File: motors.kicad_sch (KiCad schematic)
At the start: 28 parts, among them Q1 NMOS, Q2 NMOS, Q3 NMOS, Q4 NMOS

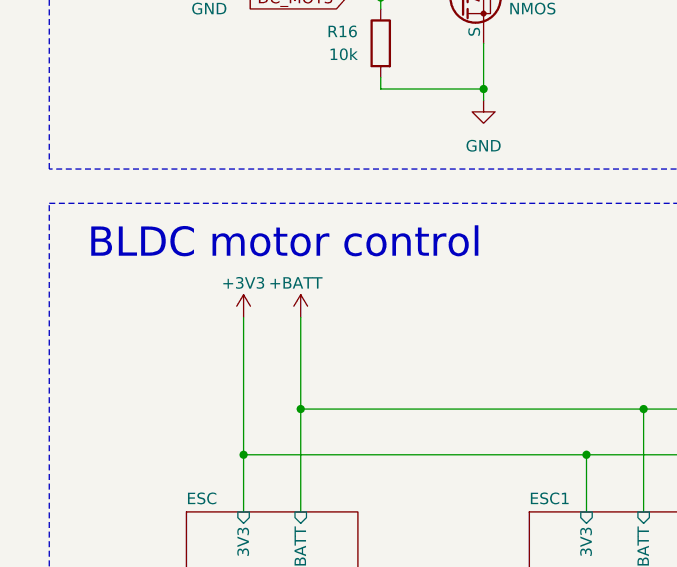
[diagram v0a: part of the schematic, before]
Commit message: Merge peripherals and sensors sheets
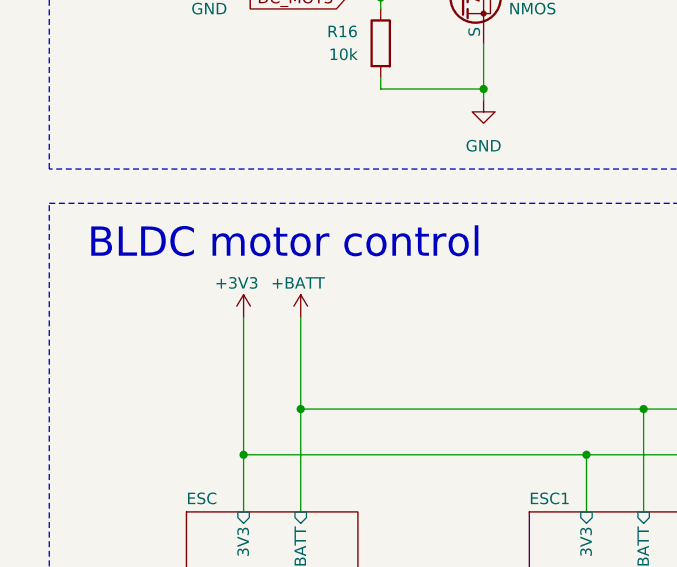
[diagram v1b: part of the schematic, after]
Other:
- company: (none) -> All-in-one drone flight controller, camera and ESC
- title: (none) -> Anticopter Duo
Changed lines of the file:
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@@
 	(generator_version "10.0")
 	(paper "A4")
+	(title_block
+		(title "Anticopter Duo")
+		(date "2026-08-28")
+		(rev "1.0")
+		(company "All-in-one drone flight controller, camera and ESC")
+		(comment 1 "ESP32 P4 + ESP32 C5, 4xAM32 ESCs")
+		(comment 2 "1S DC motors, 2S-3S BLDC motors")
+	)
 	(rectangle
 		(start 17.78 115.57)
@@
 	)
 	(junction
-		(at 39.37 143.51)
+		(at 45.72 138.43)
 		(diameter 0)
 		(color 0 0 0 0)
@@
 	)
 	(junction
-		(at 45.72 138.43)
-		(diameter 0)
-		(color 0 0 0 0)
-	)
-	(junction
 		(at 60.96 33.02)
 		(diameter 0)
@@
 	)
 	(junction
+		(at 39.37 143.51)
+		(diameter 0)
+		(color 0 0 0 0)
+	)
+	(junction
 		(at 90.17 76.2)
 		(diameter 0)
@@
 		)
 		(property "Value" "+3V3"
-			(at 39.37 124.46 0)
+			(at 38.608 124.46 0)
 			(show_name no)
 			(do_not_autoplace no)
@@
 		)
 		(property "Value" "+BATT"
-			(at 42.164 124.46 0)
+			(at 42.418 124.46 0)
 			(show_name no)
 			(do_not_autoplace no)

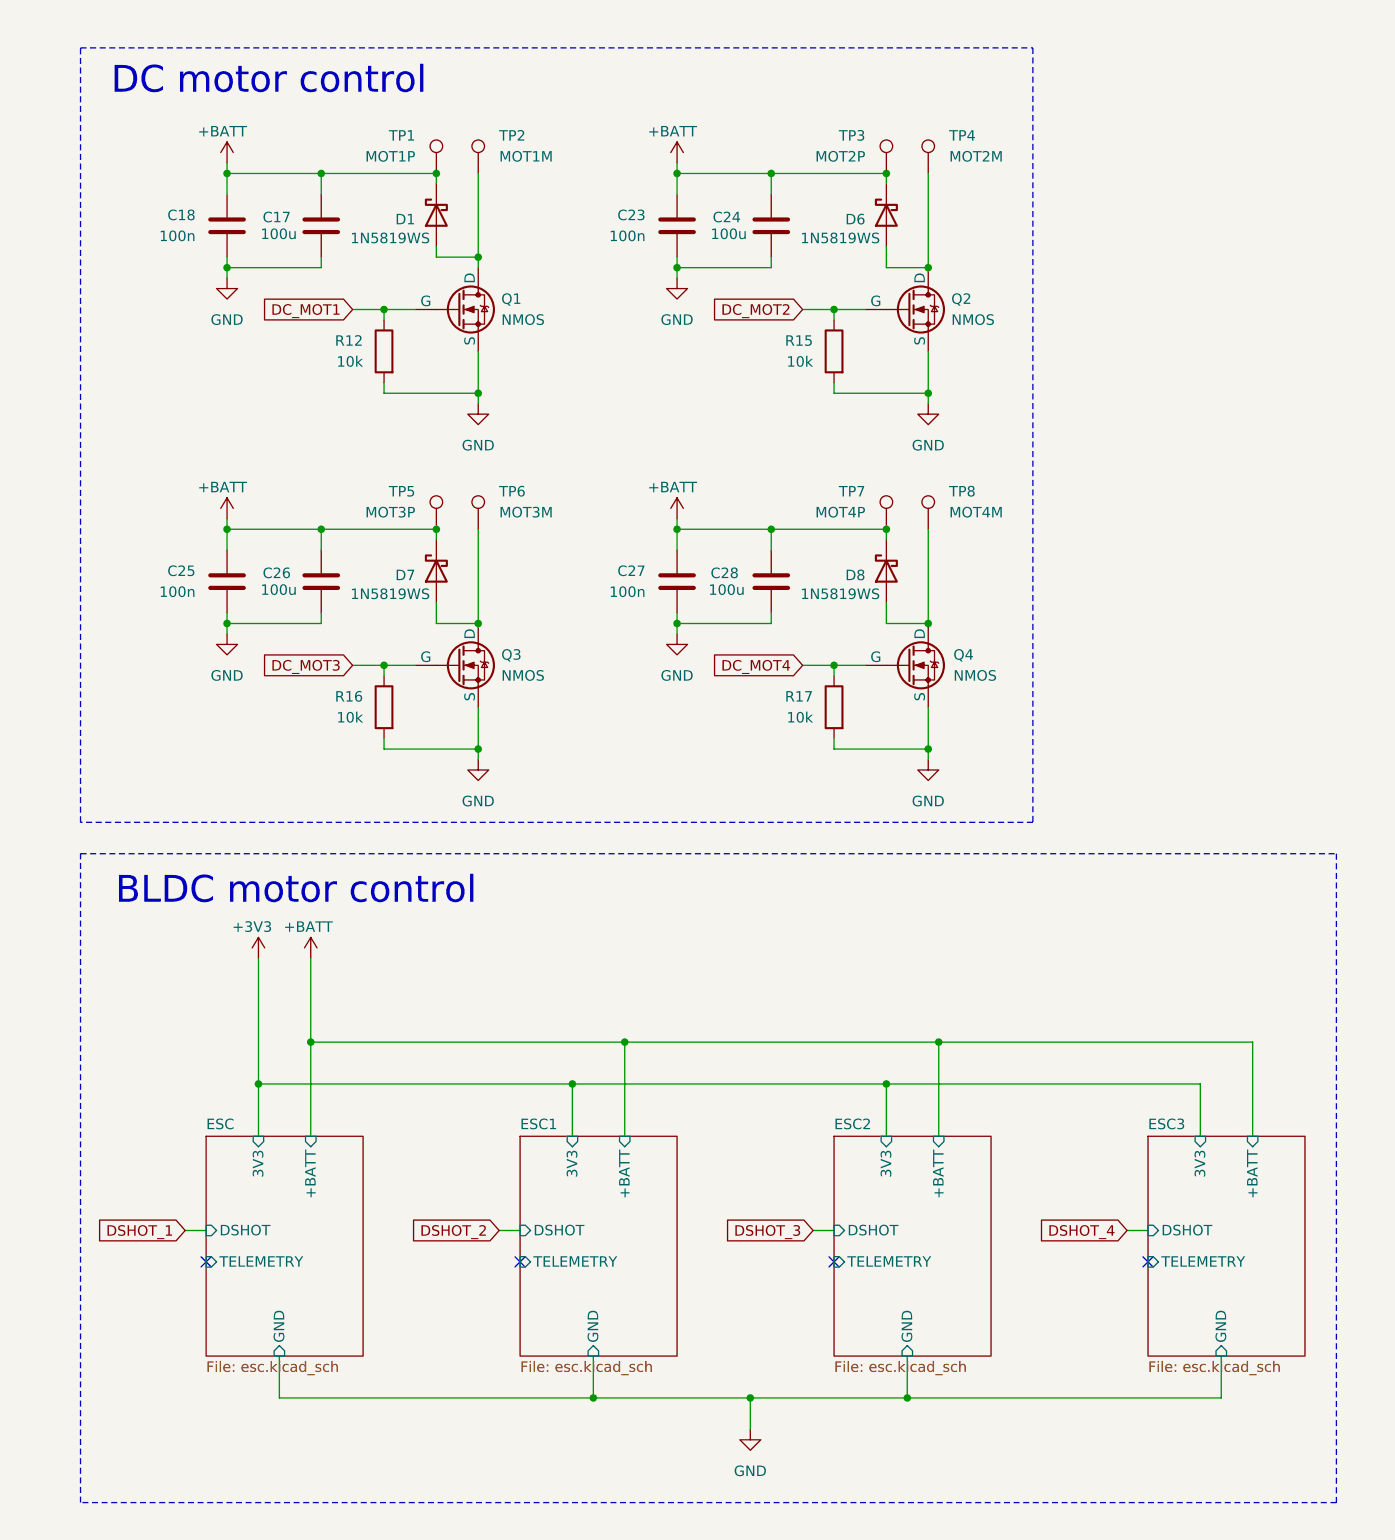
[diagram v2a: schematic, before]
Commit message: Prettify most of the schematics
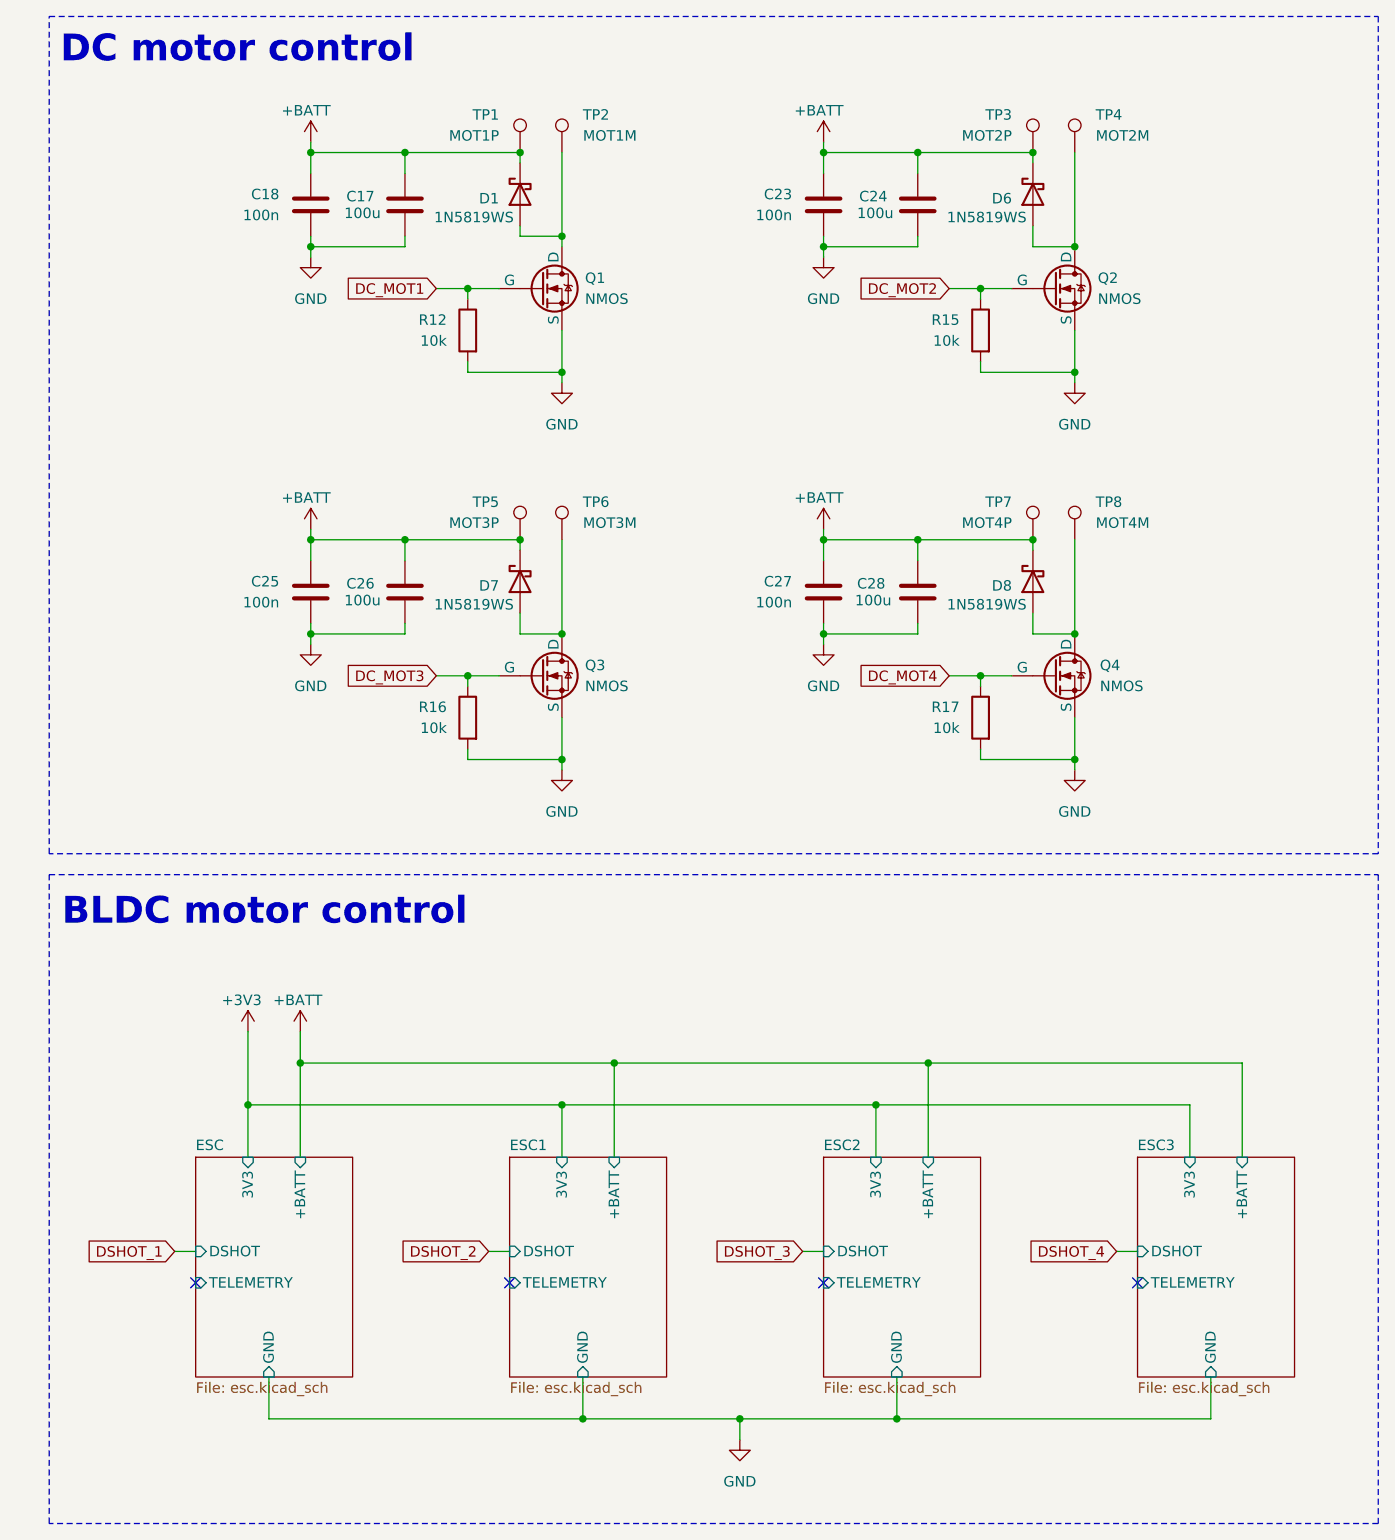
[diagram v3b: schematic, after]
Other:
- moved on the sheet: C17, C18, C23, C24, C25, C26, C27, C28, D1, D6, D7, D8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

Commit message: Various schematic improvements
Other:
- note added: "BLDC Motor Control"
- note added: "DC Motor Control"
- note removed: "BLDC motor control"
- note removed: "DC motor control"
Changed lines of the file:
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@@
 		)
 	)
-	(text "DC motor control"
+	(text "DC Motor Control"
 		(exclude_from_sim no)
 		(at 36.83 18.034 0)
@@
 		)
 	)
-	(text "BLDC motor control"
+	(text "BLDC Motor Control"
 		(exclude_from_sim no)
 		(at 40.132 122.682 0)

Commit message: Fix USB 5v -> VBUS error and some other small things
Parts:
- added R186: 10, Resistor_SMD:R_0603_1608Metric, symbol Device:R
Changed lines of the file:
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@@
 	(wire
 		(pts
-			(xy 60.96 46.99) (xy 64.77 46.99)
+			(xy 62.23 46.99) (xy 64.77 46.99)
 		)
 		(stroke
@@
 	(global_label "DC_MOT1"
 		(shape input)
-		(at 60.96 46.99 180)
+		(at 62.23 46.99 180)
 		(fields_autoplaced yes)
 		(effects
@@
 		)
 		(property "Intersheetrefs" "${INTERSHEET_REFS}"
-			(at 49.5082 46.99 0)
+			(at 50.7782 46.99 0)
 			(hide yes)
 			(show_name no)
@@
 					(unit 1)
 				)
+			)
+		)
+	)
+	(symbol
+		(lib_id "Device:R")
+		(at 55.88 64.77 270)
+		(mirror x)
+		(unit 1)
+		(body_style 1)
+		(exclude_from_sim no)
+		(in_bom yes)
+		(on_board yes)
+		(in_pos_files yes)
+		(dnp no)
+		(property "Reference" "R186"
+			(at 55.88 69.85 90)
+			(show_name no)
+			(do_not_autoplace no)
+			(effects
+				(font
+					(size 1.27 1.27)
+				)
+			)
+		)
+		(property "Value" "10"
+			(at 55.88 67.31 90)
+			(show_name no)
+			(do_not_autoplace no)
+			(effects
+				(font
+					(size 1.27 1.27)
+				)
+			)
+		)
+		(property "Footprint" "Resistor_SMD:R_0603_1608Metric"
+			(at 55.88 66.548 90)
+			(hide yes)
+			(show_name no)
+			(do_not_autoplace no)
+			(effects
+				(font
+					(size 1.27 1.27)
+				)
+			)
+		)
+		(property "Datasheet" ""
+			(at 55.88 64.77 0)
+			(hide yes)
+			(show_name no)
+			(do_not_autoplace no)
+			(effects
+				(font
+					(size 1.27 1.27)
+				)
+			)
+		)
+		(property "Description" "Resistor"
+			(at 55.88 64.77 0)
+			(hide yes)
+			(show_name no)
+			(do_not_autoplace no)
+			(effects
+				(font
+					(size 1.27 1.27)
+				)
+			)
+		)
+		(pin "2"
+		)
+		(pin "1"
+		)
+		(instances
+			(project "espdrone"
+				(path "/d7b09c1f-60ff-44c2-9b85-8e9b4c9b8de4"
+					(reference "R186")
+					(unit 1)
+				)

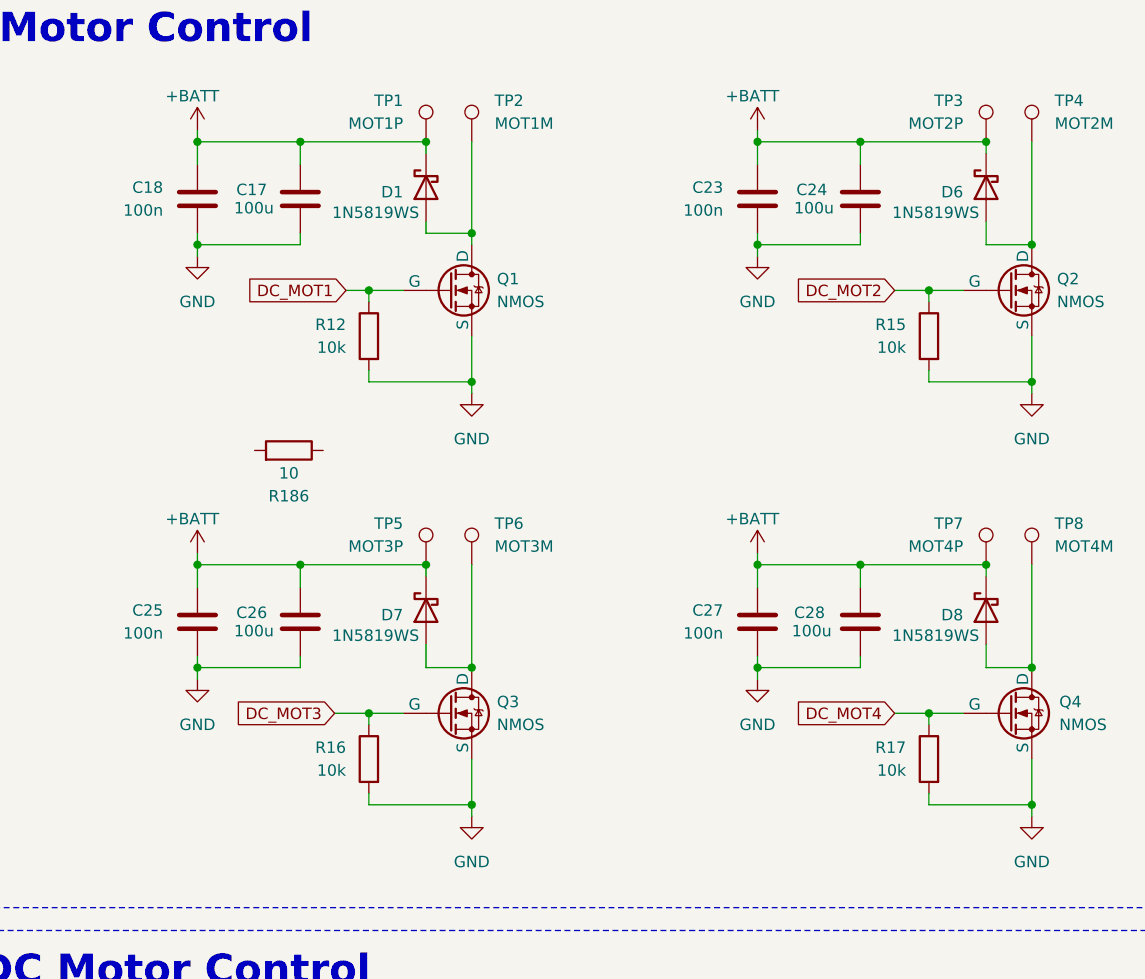
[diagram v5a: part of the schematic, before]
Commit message: Improve connectors and DC flyback diode
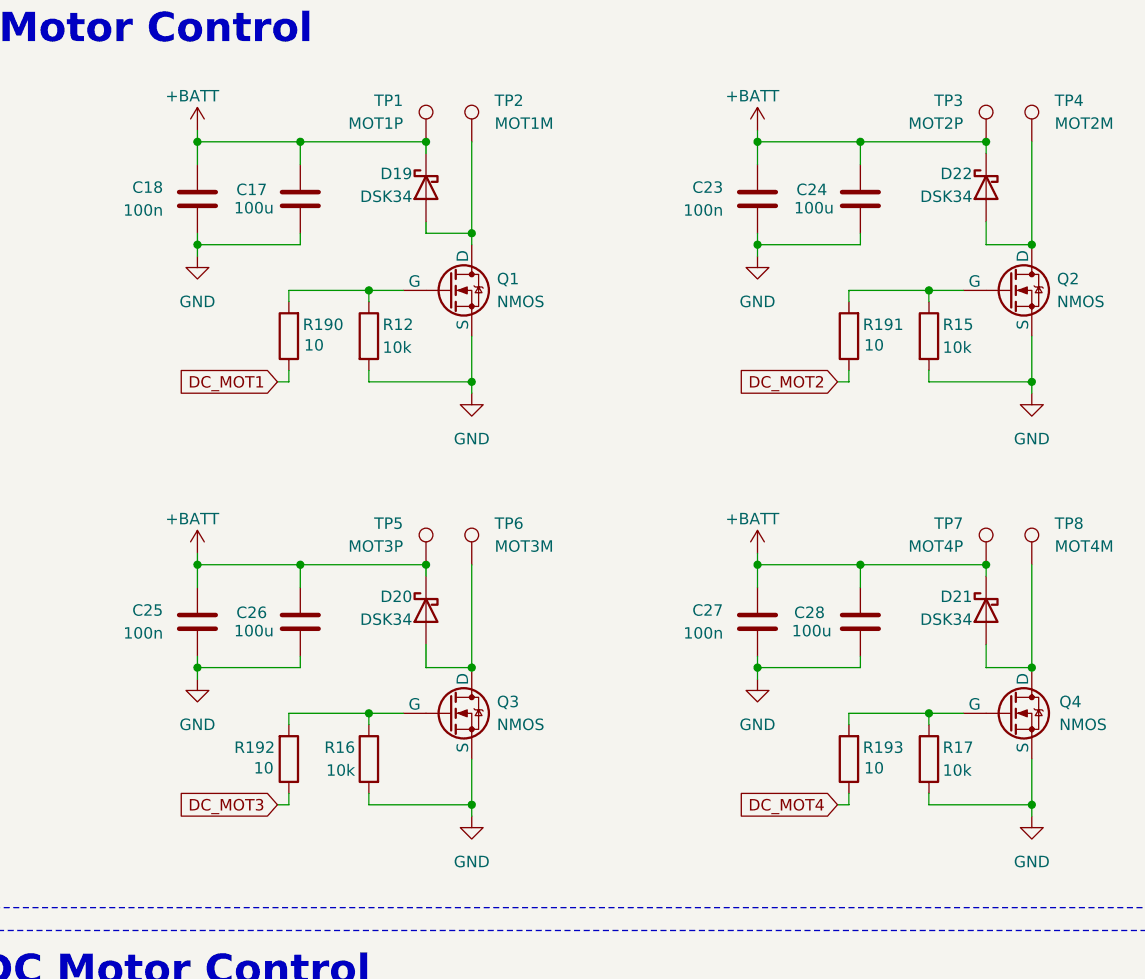
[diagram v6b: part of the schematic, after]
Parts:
- removed D1, D6, D7, D8: 1N5819WS, Diode_SMD:D_SOD-323, symbol Diode:1N5819WS
- removed R186: 10, Resistor_SMD:R_0603_1608Metric, symbol Device:R
- added D19, D20, D21, D22: DSK34, Diode_SMD:D_SOD-123F, symbol Device:D_Schottky
- added R190, R191, R192, R193: 10, Resistor_SMD:R_0603_1608Metric, symbol Device:R
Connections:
- net +BATT: now also D19.1 (K), D20.1 (K), D21.1 (K), D22.1 (K)
- net DC_MOT1: now also R190.1; no longer Q1.2 (G), R12.1
- net DC_MOT2: now also R191.1; no longer Q2.2 (G), R15.1
- net DC_MOT3: now also R192.1; no longer Q3.2 (G), R16.1
- net DC_MOT4: now also R193.1; no longer Q4.2 (G), R17.1
- net at Q1.1 (D), TP2.1: now also D19.2 (A)
- net at Q3.1 (D), TP6.1: now also D20.2 (A)
- net at Q2.1 (D), TP4.1: now also D22.2 (A)
- net at Q4.1 (D), TP8.1: now also D21.2 (A)
- new net: Q2.2 (G), R15.1, R191.2
- new net: Q1.2 (G), R12.1, R190.2
- new net: Q4.2 (G), R17.1, R193.2
- new net: Q3.2 (G), R16.1, R192.2
